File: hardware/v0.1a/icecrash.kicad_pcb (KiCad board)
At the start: 4 copper layers, 74.3 x 38 mm, 62 parts, among them J1 SNES, J2 HDMI_A, J3 pkl_jumper, J5 Conn_02x08_Odd_Even, SW1 TACT, U1 74LVC2T45, U2 74LVC2T45, U3 74LVC2T45, U4 SII902xA-mod, U5 TLV62568DBV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

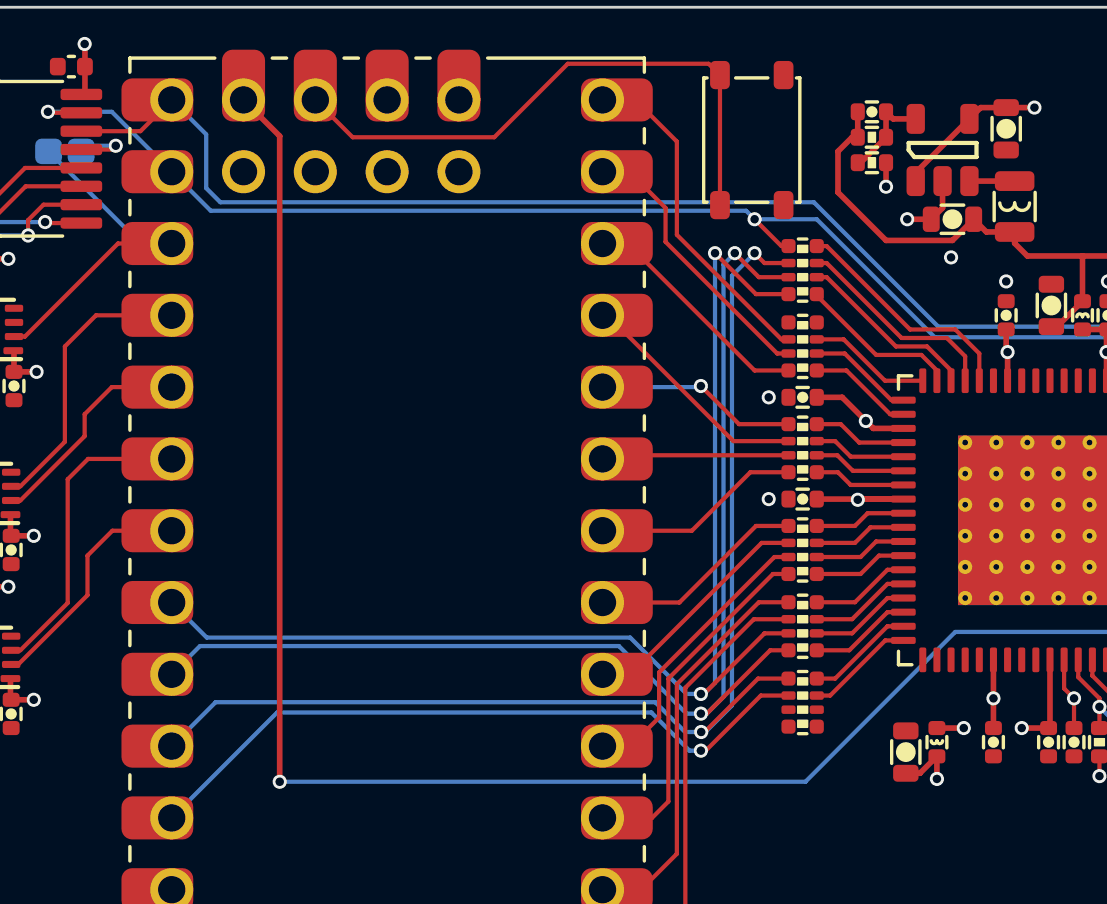
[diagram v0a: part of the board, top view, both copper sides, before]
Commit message: Changed the HDMI encoder wiring a bit.
It is better to leave the sync signals alone. We can double assign some
of the data pins to gain access to a bunch of additional video data
modes. Now `d[7:4]` are also connected to `d[15:12]`.
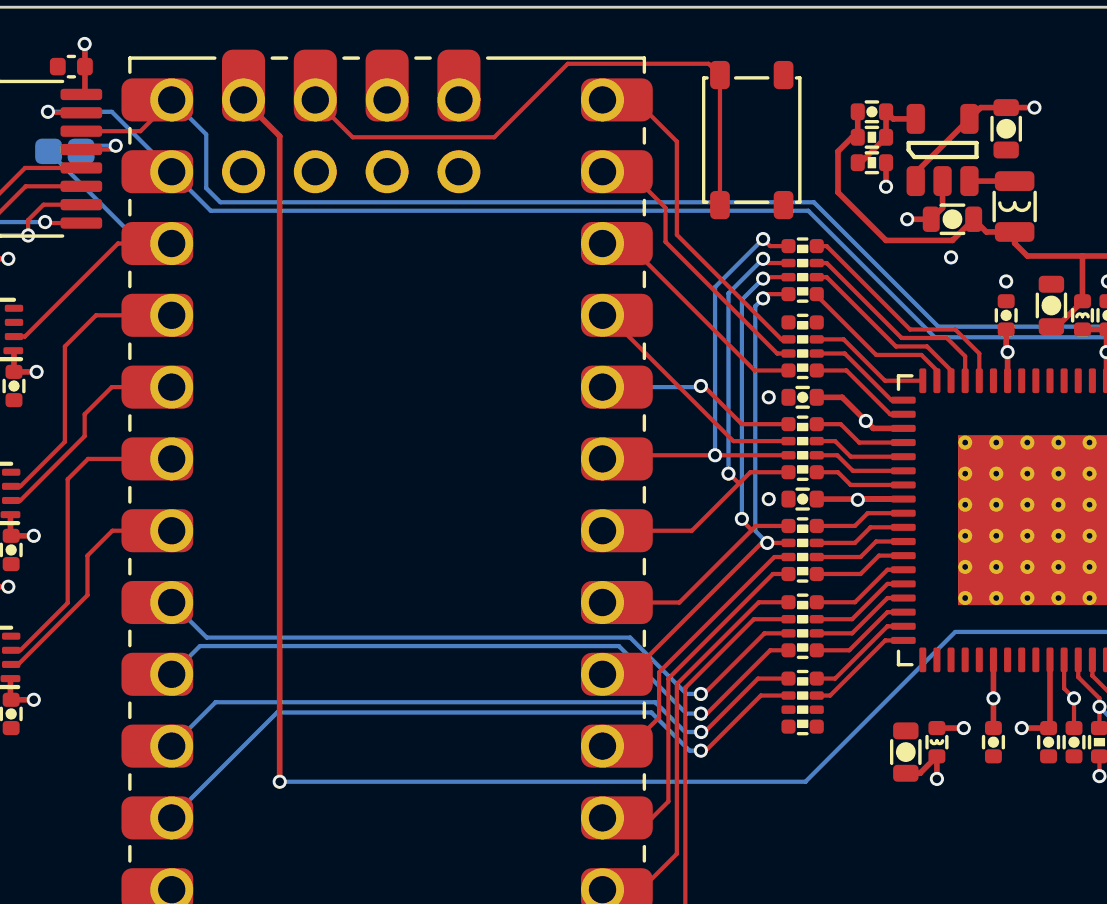
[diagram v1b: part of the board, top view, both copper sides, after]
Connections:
- net Net-(A1-Pad31) renamed /CRESET
- net Net-(R10-Pad5) renamed /iSPDIF
- net Net-(R10-Pad7) renamed /iVSYNC
- net Net-(R17-Pad2) renamed /iVD15
- net Net-(R17-Pad4) renamed /iVD14
- net Net-(R17-Pad6) renamed /iVD13
- net Net-(R17-Pad8) renamed /iVD12
- net Net-(R4-Pad2) renamed /iVD1
- net Net-(R4-Pad4) renamed /iVD0
- net Net-(R4-Pad6) renamed /iDE
- net Net-(R4-Pad8) renamed /iHSYNC
- net Net-(R5-Pad4) renamed /iVD11
- net Net-(R5-Pad6) renamed /iVD10
- net Net-(R5-Pad8) renamed /iVD9
- net Net-(R6-Pad2) renamed /iVD5
- net Net-(R6-Pad4) renamed /iVD4
- net Net-(R6-Pad6) renamed /iVD3
- net Net-(R6-Pad8) renamed /iVD2
- net Net-(R7-Pad2) renamed /iIDCK
- net Net-(R7-Pad4) renamed /iVD8
- net Net-(R7-Pad6) renamed /iVD7
- net Net-(R7-Pad8) renamed /iVD6
- A1 pad 23: /VSYNC -> /HSYNC
- A1 pad 24: /HSYNC -> /VSYNC
- J1 pad 4: /xGPDAT0 -> /xGPSEL
- J1 pad 5: /xGPDAT1 -> /xGPDAT0
- J1 pad 6: /xGPSEL -> /xGPDAT1
- R10 pad 8: /HSYNC -> /VSYNC
- R17 pad 1: /CSDA -> /VD7
- R17 pad 3: /HSYNC -> /VD6
- R17 pad 5: /VSYNC -> /VD5
- R17 pad 7: /DE -> /VD4
- R4 pad 7: /VSYNC -> /HSYNC
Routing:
- net /VSYNC: track 43.3 -> 23.8 mm, vias 2 -> 1
- net /DE: track 43.1 -> 24.2 mm, vias 2 -> 1
- net /HSYNC: track 42.8 -> 24.4 mm, vias 2 -> 1
- net /VD5: track 7.70 -> 18.0 mm, vias 0 -> 2
- net /VD4: track 8.51 -> 18.4 mm, vias 0 -> 2
- net /VD6: track 7.44 -> 17.0 mm, vias 0 -> 2
- net /VD7: track 6.63 -> 16.0 mm, vias 0 -> 2
- net /CSDA: track 47.6 -> 46.0 mm, vias 3 -> 2

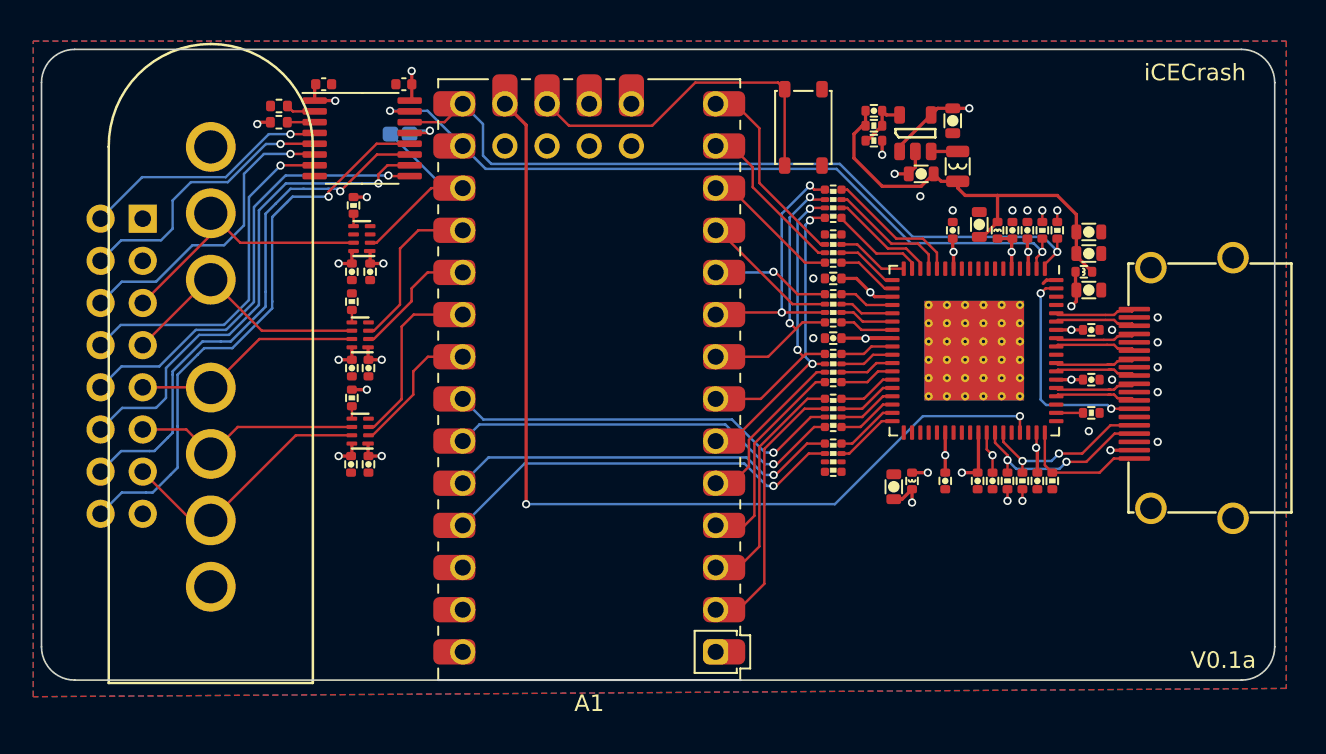
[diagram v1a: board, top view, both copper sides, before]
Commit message: More compression work. Fixed a few bugs, added silkscreen.
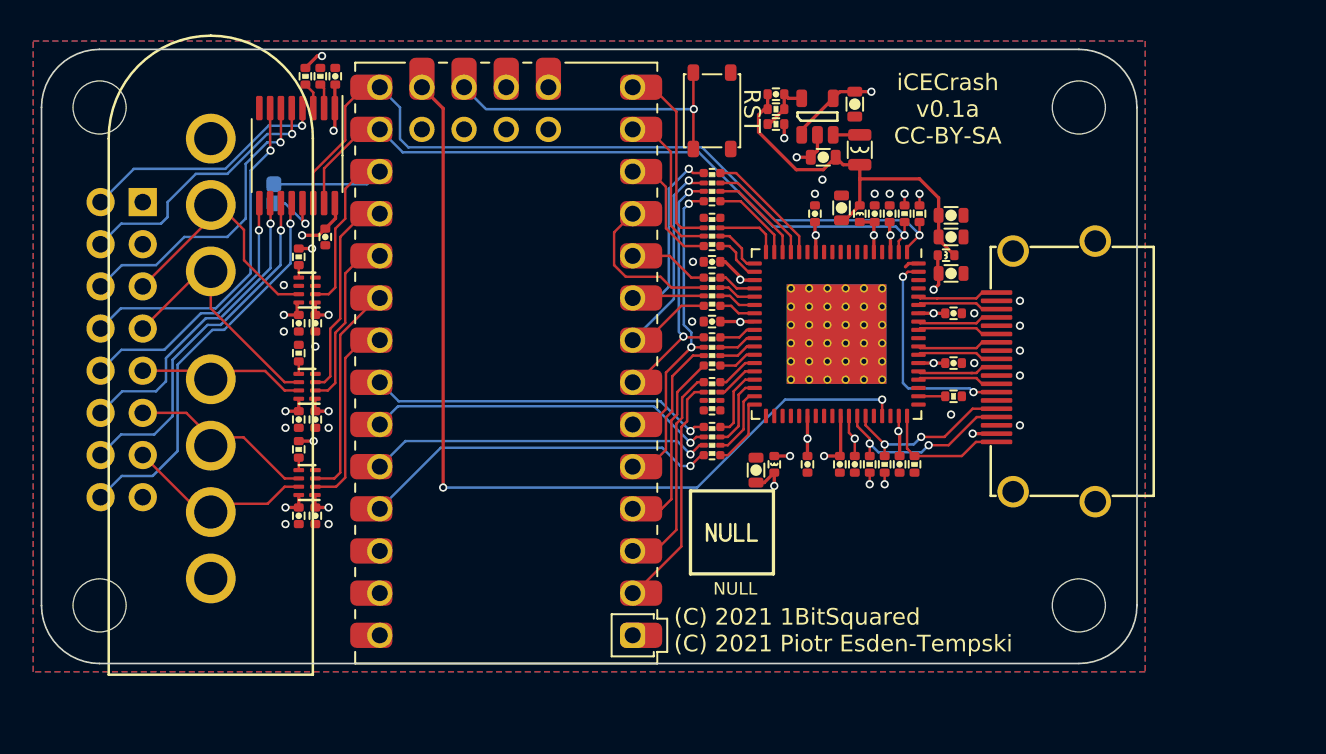
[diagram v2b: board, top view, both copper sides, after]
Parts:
- added REF**: MountingHole_3.2mm_M3, MountingHole:MountingHole_3.2mm_M3, F.Cu at (92.5, 63.5)
- added REF**: null_Logo_SilkS_5mm, pkl_logos:null_Logo_SilkS_5mm, F.Cu at (71.6, 59.1)
- added REF**: MountingHole_3.2mm_M3, MountingHole:MountingHole_3.2mm_M3, F.Cu at (92.5, 33.5)
- added REF**: MountingHole_3.2mm_M3, MountingHole:MountingHole_3.2mm_M3, F.Cu at (33.5, 63.5)
- added REF**: MountingHole_3.2mm_M3, MountingHole:MountingHole_3.2mm_M3, F.Cu at (33.5, 33.5)
- added REF**: null_Logo_SilkS_10mm, pkl_logos:null_Logo_SilkS_10mm, B.Cu at (59.6, 48.9)
- C26, C27: footprint Capacitor_SMD:C_0402_1005Metric -> pkl_dipol:C_0402
- R18, R19: footprint Resistor_SMD:R_0402_1005Metric -> pkl_dipol:R_0402
- moved C27 10.3 mm to (47.1, 41.3), turned to -90 degrees
- moved J3 8.41 mm to (44.0, 38.7), turned to -90 degrees
- moved C14 8.36 mm to (76.6, 39.9)
- moved C17 8.36 mm to (78.1, 55.0)
- moved C19 8.36 mm to (81.1, 39.9)
- moved J2 8.36 mm to (88.5, 49.4)
- moved R16 8.36 mm to (82.6, 55.0)
- moved C10 8.36 mm to (81.7, 55.0)
- moved C11 8.36 mm to (79.0, 55.0)
- moved C12 8.36 mm to (76.2, 55.0)
- moved C15 8.36 mm to (80.2, 39.9)
- moved C16 8.36 mm to (78.2, 39.5)
- moved C20 8.36 mm to (73.0, 55.4)
- moved C21 8.36 mm to (85.0, 45.9)
- moved C22 8.36 mm to (85.0, 48.9)
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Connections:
- J1 pad 4: /xGPSEL -> /xGPDAT0
- J1 pad 5: /xGPDAT0 -> /xGPDAT1
- J1 pad 6: /xGPDAT1 -> /xGPSEL
- R10 pad 1: (no net) -> /DE
- R10 pad 2: (no net) -> /iDE
- R10 pad 3: (no net) -> /HSYNC
- R10 pad 4: (no net) -> /iHSYNC
- R10 pad 5: /iSPDIF -> /VSYNC
- R10 pad 6: /SPDIF -> /iVSYNC
- R10 pad 7: /iVSYNC -> /SPDIF
- R10 pad 8: /VSYNC -> /iSPDIF
- R4 pad 5: /DE -> (no net)
- R4 pad 6: /iDE -> (no net)
- R4 pad 7: /HSYNC -> (no net)
- R4 pad 8: /iHSYNC -> (no net)
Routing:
- net /G5: track 29.9 -> 18.6 mm
- net /G4: track 27.3 -> 16.2 mm
- net /G6: track 32.1 -> 21.3 mm
- net /G7: track 34.5 -> 24.0 mm
- net +3V3: track 20.2 -> 14.1 mm
- net /xGPCLK: track 15.9 -> 11.0 mm
- net /GPSEL: track 12.6 -> 16.8 mm
- net /xGPDAT0: track 13.8 -> 9.89 mm
- net /CVCC12: track 45.5 -> 41.8 mm
- net /CSDA: track 46.0 -> 42.6 mm, vias 2 -> 1
- net /HSYNC: track 24.4 -> 21.0 mm
- net /DE: track 24.2 -> 20.8 mm
- net /CDONE/~{RST}: track 57.6 -> 54.3 mm
- net /GPCLK: track 8.46 -> 11.8 mm
- net /VSYNC: track 23.8 -> 20.7 mm
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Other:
- board size 74.3 x 38 mm -> 66 x 37 mm
- board text added: "(C) 2021 1BitSquared (C) 2021 Piotr Esden-Tempski"
- board text added: "3V3"
- board text added: "5V"
- board text added: "CDONE/~{RST}"
- board text added: "CRESET"
- board text added: "CSCL"
- board text added: "CSDA"
- board text added: "DE"
- board text added: "GND"
- board text added: "GPCLK"
- board text added: "GPD0"
- board text added: "GPD1"
- board text added: "GPLAT"
- board text added: "GPSEL"
- board text added: "HSYNC"
- board text added: "IDCK"
- board text added: "NULL"
- board text added: "RST"
- board text added: "SPDIF"
- board text added: "VD0"
- board text added: "VD1"
- board text added: "VD10"
- board text added: "VD11"
- board text added: "VD2"
- board text added: "VD3"
- board text added: "VD4/12"
- board text added: "VD5/13"
- board text added: "VD6/14"
- board text added: "VD7/15"
- board text added: "VD8"
- board text added: "VD9"
- board text added: "VSYNC"
- board text added: "iCECrash ${REVISION} CC-BY-SA"
- board text removed: "V0.1a"
- board text removed: "iCECrash"

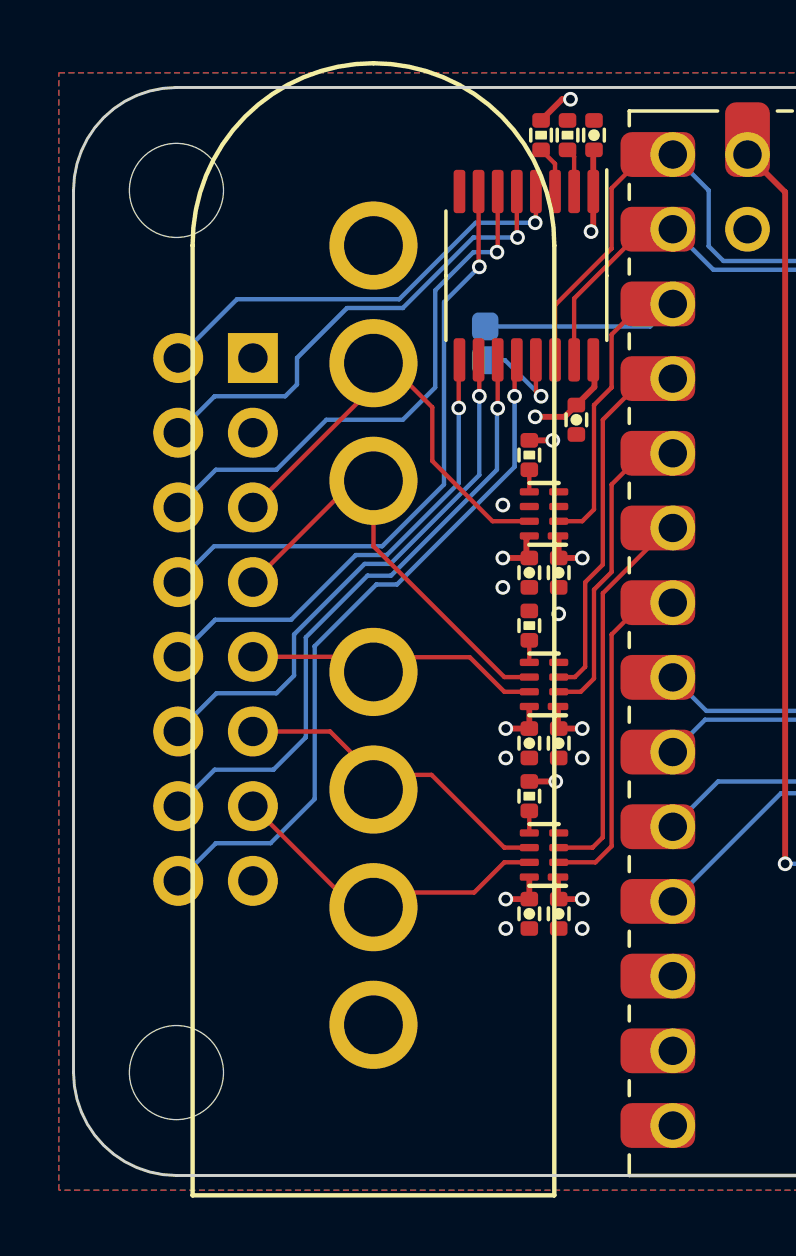
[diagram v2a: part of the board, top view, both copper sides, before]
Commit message: Aligned pin headers to the PCB center.
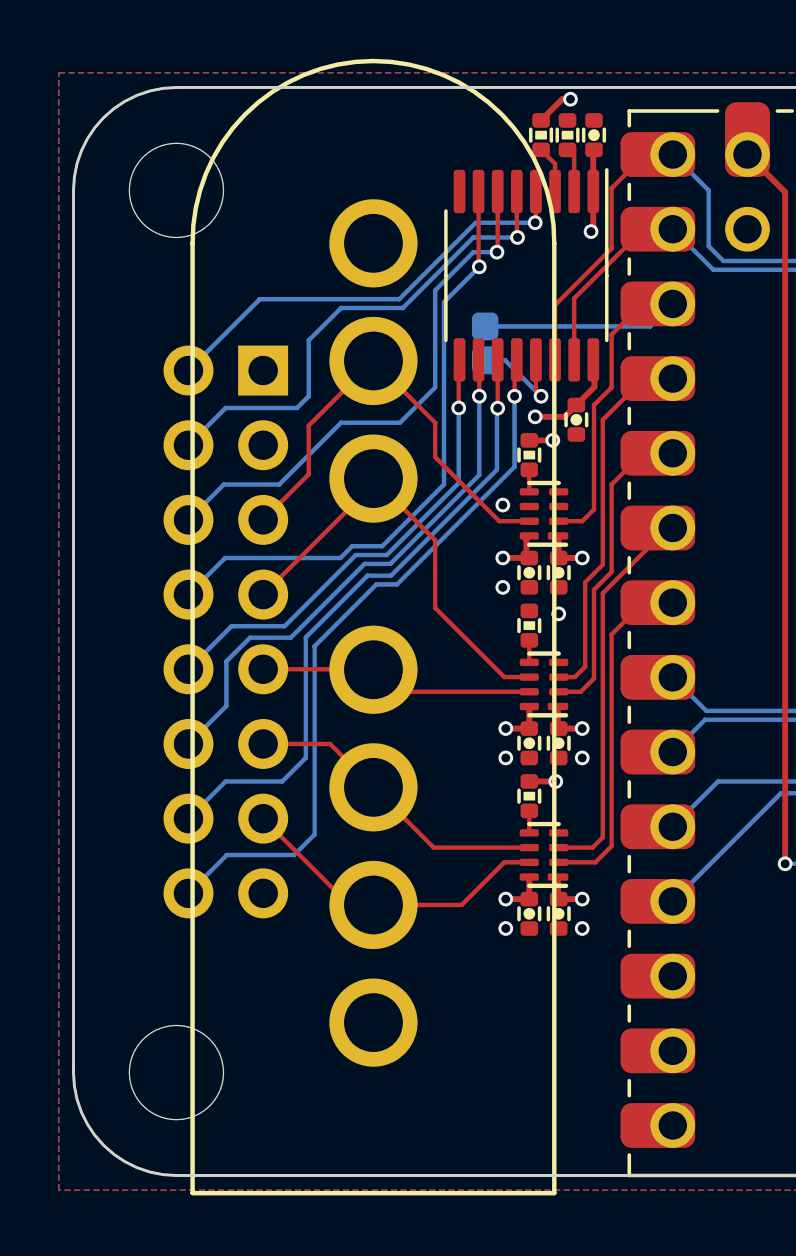
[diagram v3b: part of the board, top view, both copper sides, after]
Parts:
- moved J5 0.55 mm to (36.5, 39.6)
- moved J1 0.08 mm to (40.2, 61.8)
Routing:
- net /xGPCLK: track 11.0 -> 12.0 mm
- net /xGPSEL: track 15.9 -> 16.5 mm
- net /G7: track 24.0 -> 24.5 mm
- net /xGPLATCH: track 11.0 -> 10.5 mm
- net /xGPDAT1: track 15.6 -> 15.1 mm
- net /xGPDAT0: track 9.89 -> 9.39 mm
